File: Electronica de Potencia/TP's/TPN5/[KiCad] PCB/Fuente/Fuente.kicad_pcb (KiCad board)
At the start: 2 copper layers, 127 x 77 mm, 21 parts, among them J1 220 VAC

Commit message: actualizo fuente
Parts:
- added C10: 0.1u, Capacitor_THT:C_Rect_L16.5mm_W5.0mm_P15.00mm_MKT, F.Cu at (150.3, 38.5)
- added C11: 0.1u, Capacitor_THT:C_Rect_L16.5mm_W5.0mm_P15.00mm_MKT, F.Cu at (191.8, -0.62)
- added C12: 10u, Capacitor_THT:CP_Radial_D18.0mm_P7.50mm, F.Cu at (136.3, 25.4)
- added C13: 10u, Capacitor_THT:CP_Radial_D18.0mm_P7.50mm, F.Cu at (156.4, 5.88)
- added C15: 10u, Capacitor_THT:CP_Radial_D18.0mm_P7.50mm, F.Cu at (156.4, 25.4)
- added C7: 330u|24V, Capacitor_THT:CP_Radial_D18.0mm_P7.50mm, F.Cu at (176.4, 5.88)
- added C8: 0.1u, Capacitor_THT:C_Rect_L16.5mm_W5.0mm_P15.00mm_MKT, F.Cu at (131.6, 38.5)
- added C9: 330u|24V, Capacitor_THT:CP_Radial_D18.0mm_P7.50mm, F.Cu at (136.3, 5.88)
- added D3: DIODE, lib_fp:TO-220-3_Vertical, F.Cu at (213.6, 116.9)
- added D8: 1N4148, Diode_THT:D_DO-35_SOD27_P7.62mm_Horizontal, F.Cu at (179.5, 42.0)
- added D9: 1N4148, Diode_THT:D_DO-35_SOD27_P7.62mm_Horizontal, F.Cu at (168.8, 42.0)
- added J2: Salida +24V, lib_fp:TerminalBlock_bornier-2_P5.08mm, F.Cu at (215.2, 82.4)
- added MOD1: MP1584, lib_fp:MP1584, F.Cu at (156.2, 109.9)
- added Q1: IRF840, lib_fp:TO-220-3_Vertical, F.Cu at (189.8, 133.8)
- added Q2: IRF840, lib_fp:TO-220-3_Vertical, F.Cu at (205.8, 133.8)
- added R10: 2,2k, Resistor_THT:R_Axial_DIN0411_L9.9mm_D3.6mm_P12.70mm_Horizontal, F.Cu at (191.9, 10.4)
- added R11: 10k, Resistor_THT:R_Axial_DIN0411_L9.9mm_D3.6mm_P12.70mm_Horizontal, F.Cu at (191.9, 15.5)
- added R12: 1K, Resistor_THT:R_Axial_DIN0411_L9.9mm_D3.6mm_P12.70mm_Horizontal, F.Cu at (182.7, 20.7)
- added R13: 1,5K, Resistor_THT:R_Axial_DIN0411_L9.9mm_D3.6mm_P12.70mm_Horizontal, F.Cu at (182.7, 25.8)
- added R15: 2,2k, Resistor_THT:R_Axial_DIN0411_L9.9mm_D3.6mm_P12.70mm_Horizontal, F.Cu at (182.7, 31.0)
- added R16: 1K, Resistor_THT:R_Axial_DIN0411_L9.9mm_D3.6mm_P12.70mm_Horizontal, F.Cu at (188.5, 36.1)
- added R17: 1K, Resistor_THT:R_Axial_DIN0411_L9.9mm_D3.6mm_P12.70mm_Horizontal, F.Cu at (199.4, 20.7)
- added R7: 6,8k, Resistor_THT:R_Axial_DIN0411_L9.9mm_D3.6mm_P12.70mm_Horizontal, F.Cu at (199.4, 25.8)
- added R8: 1K, Resistor_THT:R_Axial_DIN0411_L9.9mm_D3.6mm_P12.70mm_Horizontal, F.Cu at (191.9, 5.23)
- added R9: 2,2k, Resistor_THT:R_Axial_DIN0411_L9.9mm_D3.6mm_P12.70mm_Horizontal, F.Cu at (171.9, 37.6)
- added SW1: ROCKER, lib_fp:Rocker, F.Cu at (106.0, 117.8)
- added T1: Transformer_1P_SS, lib_fp:Transformador_EE25, F.Cu at (209.2, 131.4)
- added U1: TL494, Package_DIP:DIP-16_W7.62mm_LongPads, F.Cu at (156.2, 133.2)
- added U2: IR2110, Package_DIP:DIP-14_W7.62mm, F.Cu at (168.5, 125.5)
- C5, C6: value 330u | 200V -> 330u|200V
- FL1: value choke -> Choke Coil
- moved R5 31.5 mm to (119.8, 69.0), turned to 0 degrees
- moved F1 28.9 mm to (97.4, 91.6)
- moved C3 25.2 mm to (114.0, 69.5), turned to 180 degrees
- moved C2 21.1 mm to (121.5, 83.5)
- moved FL1 18.7 mm to (113.6, 95.8)
- moved D1 13.7 mm to (128.4, 90.4)
- moved R6 11.6 mm to (132.5, 74.0), turned to 180 degrees
- moved C4 9.69 mm to (104.0, 76.2), turned to 0 degrees
- moved C1 6.10 mm to (123.0, 121.3), turned to 90 degrees
- moved TH1 5.91 mm to (122.6, 126.8)
- moved R3 4.85 mm to (114.2, 121.3)
- moved R1 4.85 mm to (118.3, 121.3)
- moved R2 4.66 mm to (116.3, 124.4)
- moved R4 4.66 mm to (112.2, 124.4)
- moved C5 4.12 mm to (139.6, 96.4), turned to 0 degrees
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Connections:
- net GND renamed VS2
- J1 pad 1: Net-(F1-Pad2) -> Net-(J1-Pad1)

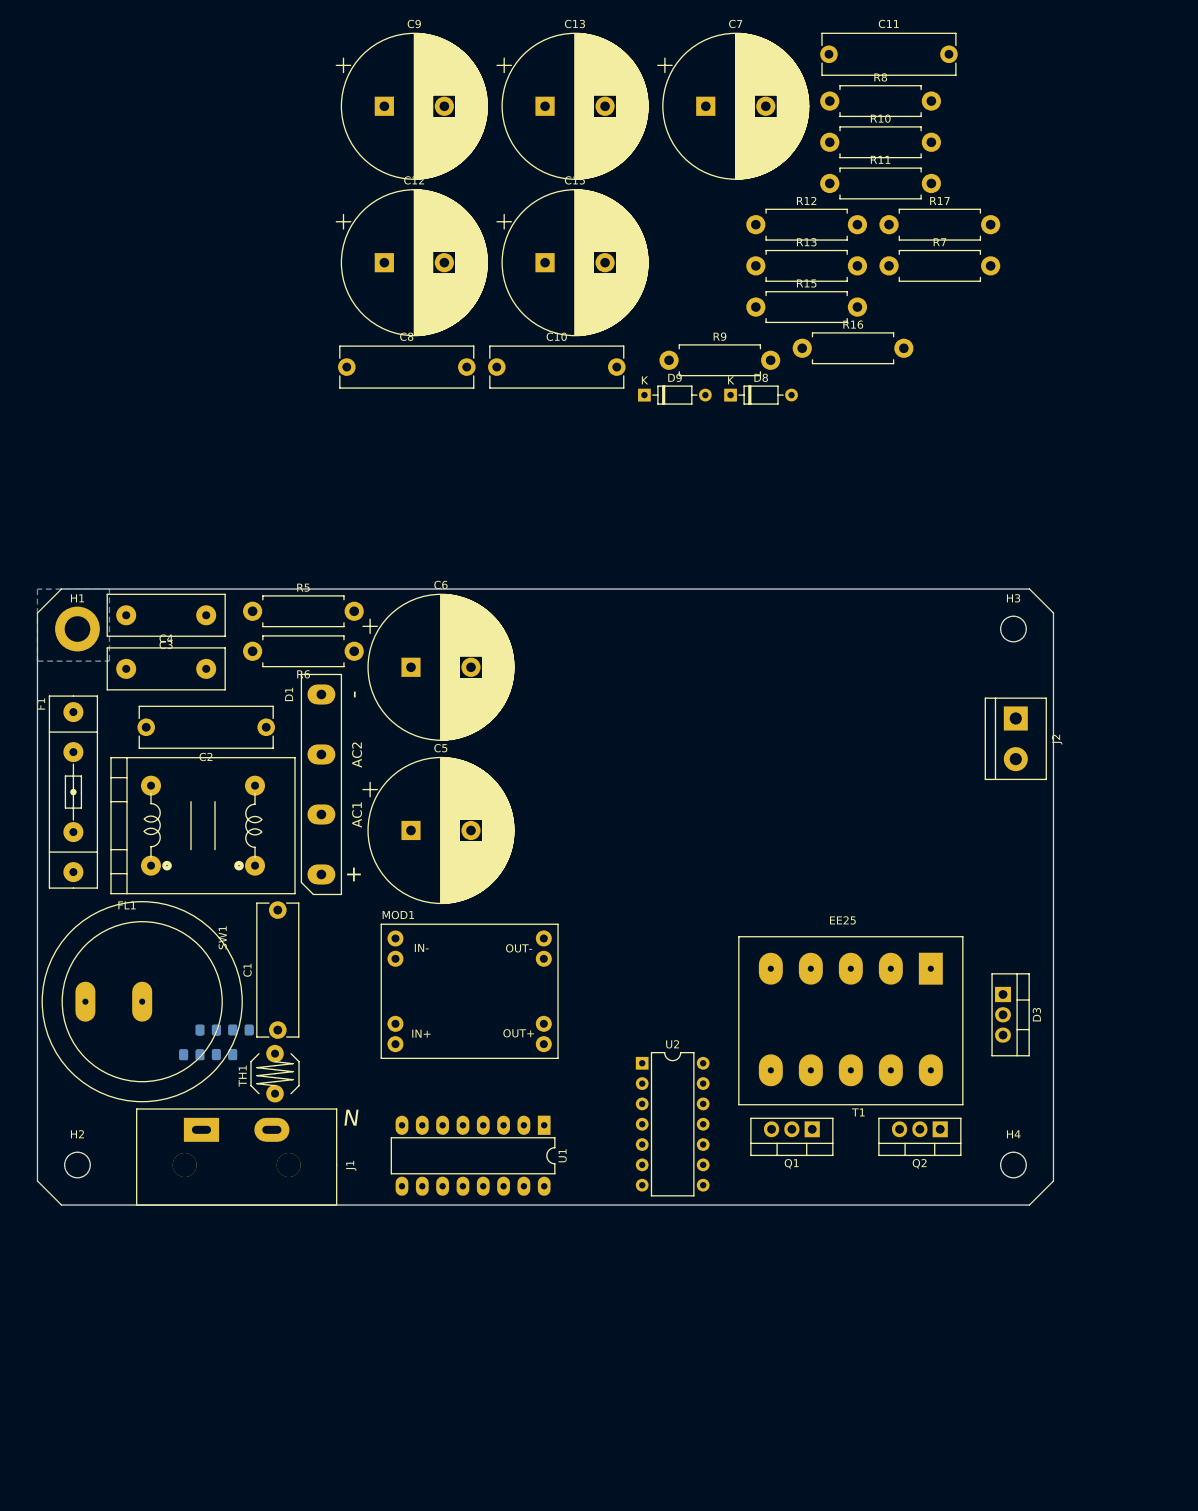
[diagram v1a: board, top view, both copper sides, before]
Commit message: Cambio el PCB de la fuente
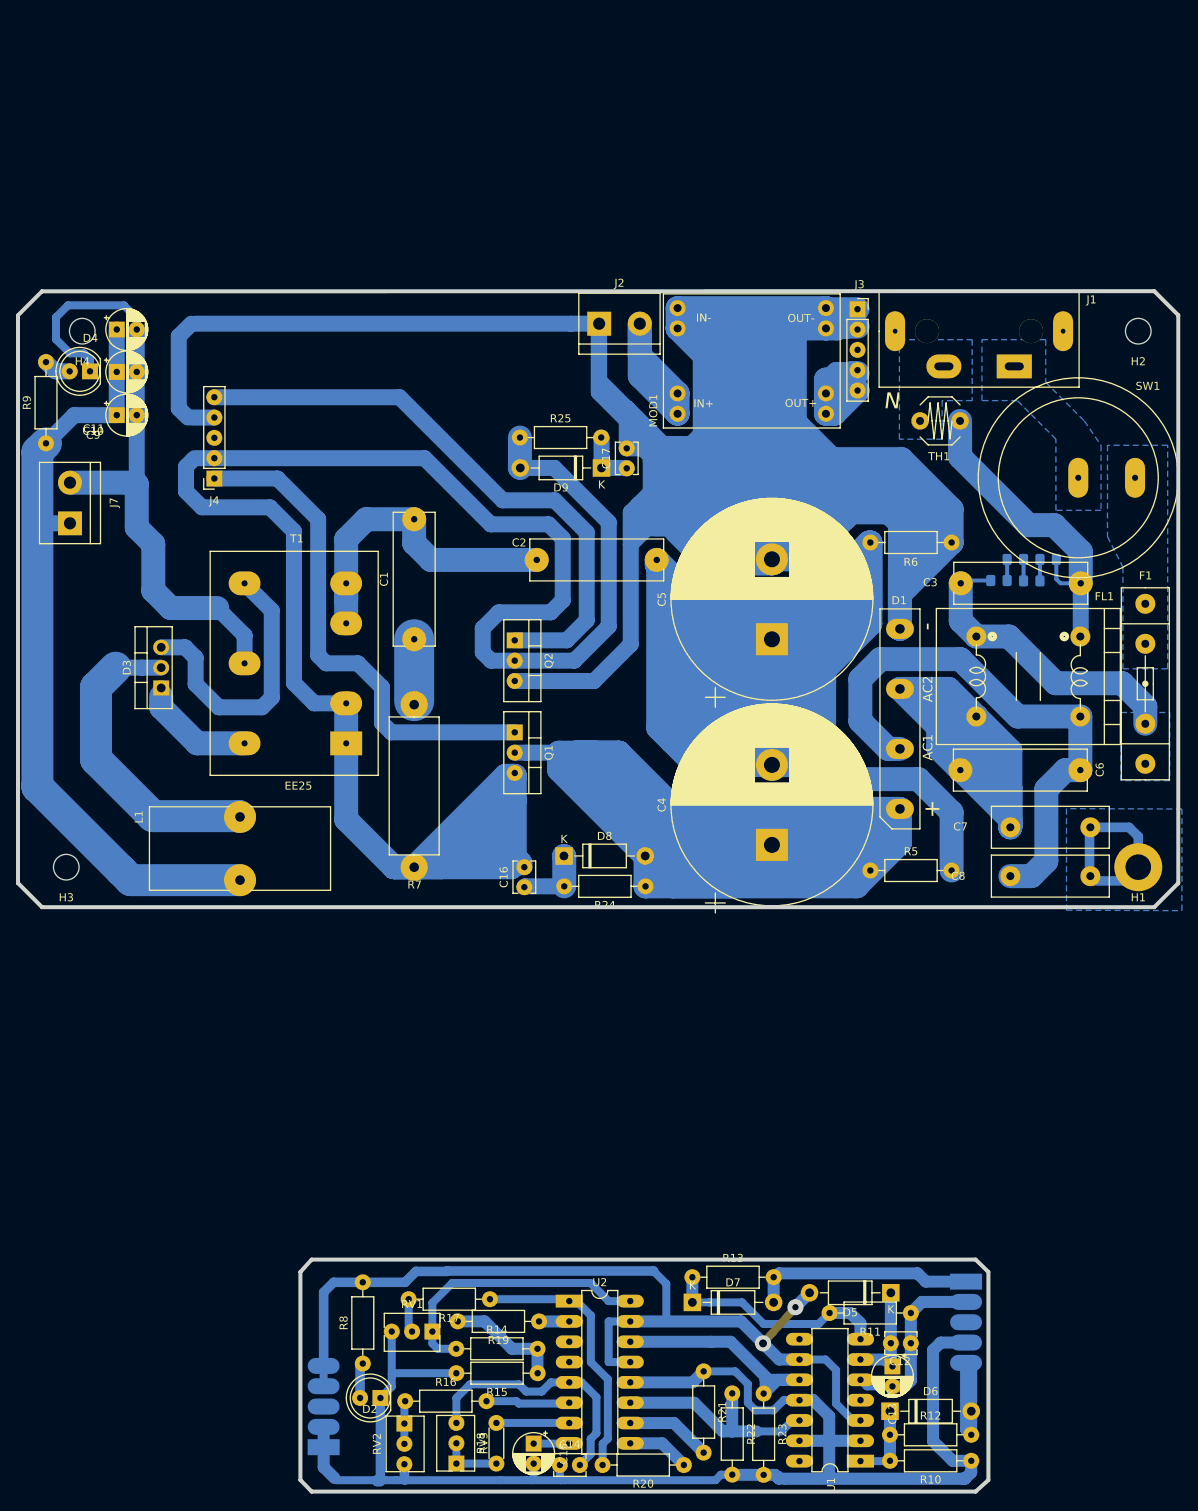
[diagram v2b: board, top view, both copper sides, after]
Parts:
- removed the C7 at (176.4, 5.88)
- removed the C8 at (131.6, 38.5)
- added C14: 2,2n, lib_fp:C_Disc_D3.8mm_W2.6mm_P2.50mm, F.Cu at (158.2, 175.7)
- added C16: 0.1u, lib_fp:C_Disc_D3.8mm_W2.6mm_P2.50mm, F.Cu at (153.8, 103.5)
- added C17: 0.1u, lib_fp:C_Disc_D3.8mm_W2.6mm_P2.50mm, F.Cu at (166.6, 51.1)
- added C3: 0.1u, lib_fp:C_Rect_L16.5mm_W5.0mm_P15.00mm_MKT, F.Cu at (208.3, 65.5)
- added C4: 330u|200V, Capacitor_THT:CP_Radial_D25.0mm_P10.00mm_SnapIn, F.Cu at (184.7, 98.2)
- added D2: G, lib_fp:LED_D5.0mm_Clear, F.Cu at (135.8, 167.3)
- added D4: Amarillo_5mm, lib_fp:LED_D5.0mm_Clear, F.Cu at (99.5, 39.0)
- added D5: MUR160, lib_fp:D_DO-41_SOD81_P10.16mm_Horizontal, F.Cu at (199.6, 154.2)
- added D6: MUR160, lib_fp:D_DO-41_SOD81_P10.16mm_Horizontal, F.Cu at (199.5, 169.0)
- added D7: MUR160, lib_fp:D_DO-41_SOD81_P10.16mm_Horizontal, F.Cu at (174.8, 155.4)
- added J3: Main_OUT, Connector_PinSocket_2.54mm:PinSocket_1x05_P2.54mm_Vertical, F.Cu at (195.4, 31.2)
- added J4: Main_IN, Connector_PinSocket_2.54mm:PinSocket_1x05_P2.54mm_Vertical, F.Cu at (115.0, 52.4)
- added J5: Ctrl_OUT, Connector_PinHeader_2.54mm:PinHeader_1x05_P2.54mm_Vertical, B.Cu at (209.0, 152.8)
- added J6: Ctrl_IN, Connector_PinHeader_2.54mm:PinHeader_1x05_P2.54mm_Vertical, B.Cu at (128.7, 173.5)
- added J7: Salida +24V, lib_fp:TerminalBlock_bornier-2_P5.08mm, F.Cu at (97.0, 58.0)
- added L1: INDUCTOR, lib_fp:L_Toroid_Vertical_L22.4mm_W10.2mm_P7.90mm_Vishay_TJ4, F.Cu at (118.2, 94.7)
- added R14: 10k, lib_fp:R_Axial_DIN0207_L6.3mm_D2.5mm_P10.16mm_Horizontal, F.Cu at (145.3, 161.2)
- added R18: 100, lib_fp:R_Axial_DIN0204_L3.6mm_D1.6mm_P5.08mm_Horizontal, F.Cu at (150.3, 175.5)
- added R19: 1k, lib_fp:R_Axial_DIN0207_L6.3mm_D2.5mm_P10.16mm_Horizontal, F.Cu at (155.6, 157.8)
- added R20: 1k, lib_fp:R_Axial_DIN0207_L6.3mm_D2.5mm_P10.16mm_Horizontal, F.Cu at (173.7, 175.7)
- added R21: 100, lib_fp:R_Axial_DIN0207_L6.3mm_D2.5mm_P10.16mm_Horizontal, F.Cu at (176.2, 164.0)
- added R22: 1k, lib_fp:R_Axial_DIN0207_L6.3mm_D2.5mm_P10.16mm_Horizontal, F.Cu at (179.8, 166.8)
- added R23: 1k, lib_fp:R_Axial_DIN0207_L6.3mm_D2.5mm_P10.16mm_Horizontal, F.Cu at (183.7, 166.8)
- added R24: 10k, lib_fp:R_Axial_DIN0207_L6.3mm_D2.5mm_P10.16mm_Horizontal, F.Cu at (168.9, 103.4)
- added R25: 10k, lib_fp:R_Axial_DIN0207_L6.3mm_D2.5mm_P10.16mm_Horizontal, F.Cu at (153.2, 47.3)
- added RV1: 10k, lib_fp:Potentiometer_Bourns_3266Y_Vertical, F.Cu at (142.3, 159.0)
- added RV2: 200k, lib_fp:Potentiometer_Bourns_3266Y_Vertical, F.Cu at (138.8, 170.5)
- added RV3: 500, lib_fp:Potentiometer_Bourns_3266Y_Vertical, F.Cu at (145.3, 175.5)
- C1: value 0.1u -> 330nF|400V; footprint Capacitor_THT:C_Rect_L16.5mm_W5.0mm_P15.00mm_MKT -> lib_fp:C_Rect_L16.5mm_W5.0mm_P15.00mm_MKT
- C10, C11: value 0.1u -> 10u|50V; footprint Capacitor_THT:C_Rect_L16.5mm_W5.0mm_P15.00mm_MKT -> lib_fp:CP_Radial_D5.0mm_P2.50mm
- C12: value 10u -> 0.1u; footprint Capacitor_THT:CP_Radial_D18.0mm_P7.50mm -> lib_fp:C_Disc_D3.8mm_W2.6mm_P2.50mm
- C13: value 10u -> 22u; footprint Capacitor_THT:CP_Radial_D18.0mm_P7.50mm -> lib_fp:CP_Radial_D5.0mm_P2.50mm
- C15: footprint Capacitor_THT:CP_Radial_D18.0mm_P7.50mm -> lib_fp:CP_Radial_D5.0mm_P2.50mm
- C2: footprint Capacitor_THT:C_Rect_L16.5mm_W5.0mm_P15.00mm_MKT -> lib_fp:C_Rect_L16.5mm_W5.0mm_P15.00mm_MKT
- C5: footprint Capacitor_THT:CP_Radial_D18.0mm_P7.50mm -> Capacitor_THT:CP_Radial_D25.0mm_P10.00mm_SnapIn
- C6: value 330u|200V -> 0.1u; footprint Capacitor_THT:CP_Radial_D18.0mm_P7.50mm -> lib_fp:C_Rect_L16.5mm_W5.0mm_P15.00mm_MKT
- C9: value 330u|24V -> 10u|50V; footprint Capacitor_THT:CP_Radial_D18.0mm_P7.50mm -> lib_fp:CP_Radial_D5.0mm_P2.50mm
- D3: value DIODE -> MUR1660
- D8, D9: value 1N4148 -> MUR160; footprint Diode_THT:D_DO-35_SOD27_P7.62mm_Horizontal -> lib_fp:D_DO-41_SOD81_P10.16mm_Horizontal
- F1: footprint lib_fp:fuse_4pin_A -> lib_fp:Fuse_4pin_A
- H1: footprint MountingHole:MountingHole_3.2mm_M3_DIN965_Pad -> lib_fp:MountingHole_3.2mm_M3_DIN965_Pad
- H2, H3, H4: footprint MountingHole:MountingHole_3.2mm_M3_DIN965 -> lib_fp:MountingHole_3.2mm_M3_DIN965
- J2: value Salida +24V -> Entrada +20 V
- R1, R2, R3, R4: footprint Resistor_SMD:R_0805_2012Metric_Pad1.15x1.40mm_HandSolder -> lib_fp:R_0805_2012Metric_Pad1.15x1.40mm_HandSolder
- R10: value 2,2k -> 1k; footprint Resistor_THT:R_Axial_DIN0411_L9.9mm_D3.6mm_P12.70mm_Horizontal -> lib_fp:R_Axial_DIN0207_L6.3mm_D2.5mm_P10.16mm_Horizontal
- R11: value 10k -> 1k; footprint Resistor_THT:R_Axial_DIN0411_L9.9mm_D3.6mm_P12.70mm_Horizontal -> lib_fp:R_Axial_DIN0207_L6.3mm_D2.5mm_P10.16mm_Horizontal
- R12: value 1K -> 100; footprint Resistor_THT:R_Axial_DIN0411_L9.9mm_D3.6mm_P12.70mm_Horizontal -> lib_fp:R_Axial_DIN0207_L6.3mm_D2.5mm_P10.16mm_Horizontal
- R13: value 1,5K -> 100; footprint Resistor_THT:R_Axial_DIN0411_L9.9mm_D3.6mm_P12.70mm_Horizontal -> lib_fp:R_Axial_DIN0207_L6.3mm_D2.5mm_P10.16mm_Horizontal
- R15, R9: value 2,2k -> 10k; footprint Resistor_THT:R_Axial_DIN0411_L9.9mm_D3.6mm_P12.70mm_Horizontal -> lib_fp:R_Axial_DIN0207_L6.3mm_D2.5mm_P10.16mm_Horizontal
- R16: value 1K -> 10k; footprint Resistor_THT:R_Axial_DIN0411_L9.9mm_D3.6mm_P12.70mm_Horizontal -> lib_fp:R_Axial_DIN0207_L6.3mm_D2.5mm_P10.16mm_Horizontal
- R17: value 1K -> 1k; footprint Resistor_THT:R_Axial_DIN0411_L9.9mm_D3.6mm_P12.70mm_Horizontal -> lib_fp:R_Axial_DIN0207_L6.3mm_D2.5mm_P10.16mm_Horizontal
- R5, R6: footprint Resistor_THT:R_Axial_DIN0411_L9.9mm_D3.6mm_P12.70mm_Horizontal -> lib_fp:R_Axial_DIN0207_L6.3mm_D2.5mm_P10.16mm_Horizontal
- R7: value 6,8k -> 56|3W; footprint Resistor_THT:R_Axial_DIN0411_L9.9mm_D3.6mm_P12.70mm_Horizontal -> lib_fp:R_Axial_DIN0617_L17.0mm_D6.0mm_P20.32mm_Horizontal
- R8: value 1K -> 2,2k; footprint Resistor_THT:R_Axial_DIN0411_L9.9mm_D3.6mm_P12.70mm_Horizontal -> lib_fp:R_Axial_DIN0207_L6.3mm_D2.5mm_P10.16mm_Horizontal
- U1: value TL494 -> IR2110; footprint Package_DIP:DIP-16_W7.62mm_LongPads -> lib_fp:DIP-14_W7.62mm_LongPads
- U2: value IR2110 -> SG3525; footprint Package_DIP:DIP-14_W7.62mm -> lib_fp:DIP-16_W7.62mm_LongPads
- moved H2 168.7 mm to (230.5, 34.0), turned to 180 degrees
- moved R8 168.3 mm to (133.6, 163.0), turned to 90 degrees
- moved R10 165.8 mm to (209.6, 175.2), turned to 180 degrees
- moved C13 163.4 mm to (199.8, 163.4), turned to 270 degrees
- moved H4 156.2 mm to (98.5, 34.0), turned to 180 degrees
- moved R12 152.2 mm to (199.5, 171.9)
- moved C12 149.2 mm to (199.6, 160.5)
- moved C15 147.6 mm to (154.9, 173.0), turned to 270 degrees
- moved R17 143.3 mm to (149.5, 155.0), turned to 180 degrees
- moved R11 141.6 mm to (202.1, 156.7), turned to 180 degrees
- moved R16 140.7 mm to (138.9, 167.7)
- moved J1 139.6 mm to (210.6, 34.0), turned to 0 degrees
- moved R15 136.0 mm to (155.4, 164.2), turned to 180 degrees
- moved H1 135.9 mm to (230.5, 101.0), turned to 180 degrees
- moved F1 134.7 mm to (231.4, 78.1), turned to 90 degrees
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- renumbered C3 to C7, C4 to C8
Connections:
- C10 pad 2: Net-(C10-Pad2) -> GNDREF
- C11 pad 1: Net-(C10-Pad2) -> Net-(C10-Pad1)
- C11 pad 2: Net-(C11-Pad2) -> GNDREF
- C12 pad 2: GNDREF -> VS1_CTRL
- C13 pad 2: GNDREF -> VS1_CTRL
- C15 pad 1: Net-(C12-Pad1) -> Net-(C15-Pad1)
- C15 pad 2: GNDREF -> VS2_CTRL
- C2 pad 1: F -> Net-(C1-Pad2)
- C2 pad 2: N -> Vin|2
- C5 pad 1: Vin -> Vin|2
- C5 pad 2: Vin|2 -> VS2
- C6 pad 1: Vin|2 -> F
- C6 pad 2: VS2 -> N
- C9 pad 1: +15V -> Net-(C10-Pad1)
- C9 pad 2: VS2 -> GNDREF
- D3 pad 1: Net-(C10-Pad1) -> Net-(D3-Pad1)
- D3 pad 2: Net-(C10-Pad2) -> Net-(D3-Pad2)
- D3 pad 3: (no net) -> Net-(D3-Pad3)
- D8 pad 1: Net-(D8-Pad1) -> Net-(C16-Pad1)
- D8 pad 2: VG1 -> Vin
- D9 pad 1: Net-(D9-Pad1) -> Net-(C17-Pad1)
- D9 pad 2: VG2 -> VS1
- F1 pad 1: Net-(C1-Pad1) -> Net-(C3-Pad1)
- FL1 pad 1: Net-(C1-Pad1) -> Net-(C3-Pad1)
- FL1 pad 3: Net-(C1-Pad2) -> Net-(C3-Pad2)
- J2 pad 1: Net-(C12-Pad1) -> VS2
- J2 pad 2: GNDREF -> Net-(J2-Pad2)
- MOD1 pad 2: Net-(C7-Pad1) -> Net-(J2-Pad2)
- MOD1 pad 3: +15V -> Vin_EXT
- R1 pad 1: Net-(C1-Pad1) -> Net-(C3-Pad1)
- R10 pad 1: +5V_REF -> VS2_CTRL
- R10 pad 2: (no net) -> Net-(D6-Pad1)
- R11 pad 1: (no net) -> VS1_CTRL
- R11 pad 2: VS2 -> Net-(D7-Pad1)
- R12 pad 1: +5V_REF -> Net-(D6-Pad1)
- R12 pad 2: VS2 -> VG2_CTRL
- R13 pad 1: Net-(R13-Pad1) -> Net-(D7-Pad1)
- R13 pad 2: (no net) -> VG1_CTRL
- R15 pad 1: (no net) -> Net-(R14-Pad2)
- R15 pad 2: (no net) -> VS2_CTRL
- R16 pad 1: PWM_A -> Net-(R16-Pad1)
- R16 pad 2: VS2 -> Net-(R16-Pad2)
- R17 pad 1: PWM_B -> Net-(R17-Pad1)
- R17 pad 2: VS2 -> Net-(R17-Pad2)
- R4 pad 2: Net-(C1-Pad2) -> Net-(C3-Pad2)
- R7 pad 1: Vin|2 -> VS1
- R7 pad 2: Net-(C7-Pad1) -> Net-(C1-Pad1)
- R8 pad 1: Net-(C7-Pad1) -> Net-(D2-Pad2)
- R8 pad 2: VS2 -> Vin_CTRL
- R9 pad 1: +15V -> Net-(C10-Pad1)
- R9 pad 2: (no net) -> Net-(D4-Pad2)
- T1 pad 2: Net-(C8-Pad1) -> Net-(C1-Pad2)
- T1 pad 3: Net-(C11-Pad2) -> Net-(D3-Pad3)
- TH1 pad 2: Net-(C1-Pad2) -> Net-(C3-Pad2)
- U1 pad 1: VS2 -> Net-(D6-Pad1)
- U1 pad 11: +15V -> VS2_CTRL
- U1 pad 12: +15V -> PWM_A
- U1 pad 13: +5V_REF -> VS2_CTRL
- U1 pad 14: +5V_REF -> (no net)
- U1 pad 2: +5V_REF -> VS2_CTRL
- U1 pad 3: (no net) -> Vin_CTRL
- U1 pad 4: VS2 -> (no net)
- U1 pad 5: (no net) -> VS1_CTRL
- U1 pad 6: Net-(R13-Pad1) -> Net-(C12-Pad1)
- U1 pad 7: VS2 -> Net-(D7-Pad1)
- U1 pad 8: +15V -> (no net)
- U1 pad 9: PWM_A -> Vin_CTRL
- U2 pad 1: Net-(D9-Pad1) -> Net-(R17-Pad1)
- U2 pad 10: PWM_A -> Net-(R21-Pad2)
- U2 pad 11: VS2 -> PWM_A
- U2 pad 12: PWM_B -> VS2_CTRL
- U2 pad 13: VS2 -> Vin_CTRL
- U2 pad 14: (no net) -> PWM_B
- U2 pad 2: VS2 -> Net-(R19-Pad1)
- U2 pad 3: +15V -> (no net)
- U2 pad 5: VS1 -> Net-(C14-Pad2)
- U2 pad 6: (no net) -> Net-(R16-Pad2)
- U2 pad 7: Net-(D8-Pad1) -> Net-(R18-Pad2)
- U2 pad 8: (no net) -> Net-(C15-Pad1)
- U2 pad 9: +15V -> Net-(R20-Pad1)
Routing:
- net VS2: track 0.00 -> 682.8 mm
- net Vin: track 0.00 -> 414.9 mm
- net Vin|2: track 0.00 -> 351.5 mm
- net VS1: track 0.00 -> 324.3 mm
- net VS2_CTRL: track 0.00 -> 232.3 mm
- net Net-(C10-Pad1): track 0.00 -> 173.6 mm
- net Vin_CTRL: track 0.00 -> 134.2 mm, vias 0 -> 2
- net F: track 0.00 -> 90.4 mm
- net GNDREF: track 0.00 -> 81.5 mm
- net VG2: track 0.00 -> 74.6 mm
- net N: track 0.00 -> 69.4 mm
- net VG1: track 0.00 -> 63.3 mm
- net VG1_CTRL: track 0.00 -> 49.5 mm
- net PWM_B: track 0.00 -> 43.5 mm
- net Net-(C1-Pad2): track 0.00 -> 41.3 mm
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- added copper zone on B.Cu, net Net-(C3-Pad1)
- added copper zone on B.Cu, net Net-(F1-Pad2)
- added copper zone on B.Cu, net Net-(J1-Pad1)
- added copper zone on B.Cu, net Net-(J1-Pad2)
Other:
- board size 127 x 77 mm -> 145 x 150.1 mm
- net class Default: clearance 0.2 -> 0.4; trace_width 0.25 -> 1.2; via_dia 0.8 -> 1.5; via_drill 0.4 -> 1
- rule trace_clearance: 0.2 -> 0.4
- rule trace_min: 0.2 -> 0.4
- rule via_min_drill: 0.3 -> 0.8
- rule via_min_size: 0.4 -> 1.5
